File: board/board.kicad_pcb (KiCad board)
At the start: 2 copper layers, 21 x 13 mm, 1 part

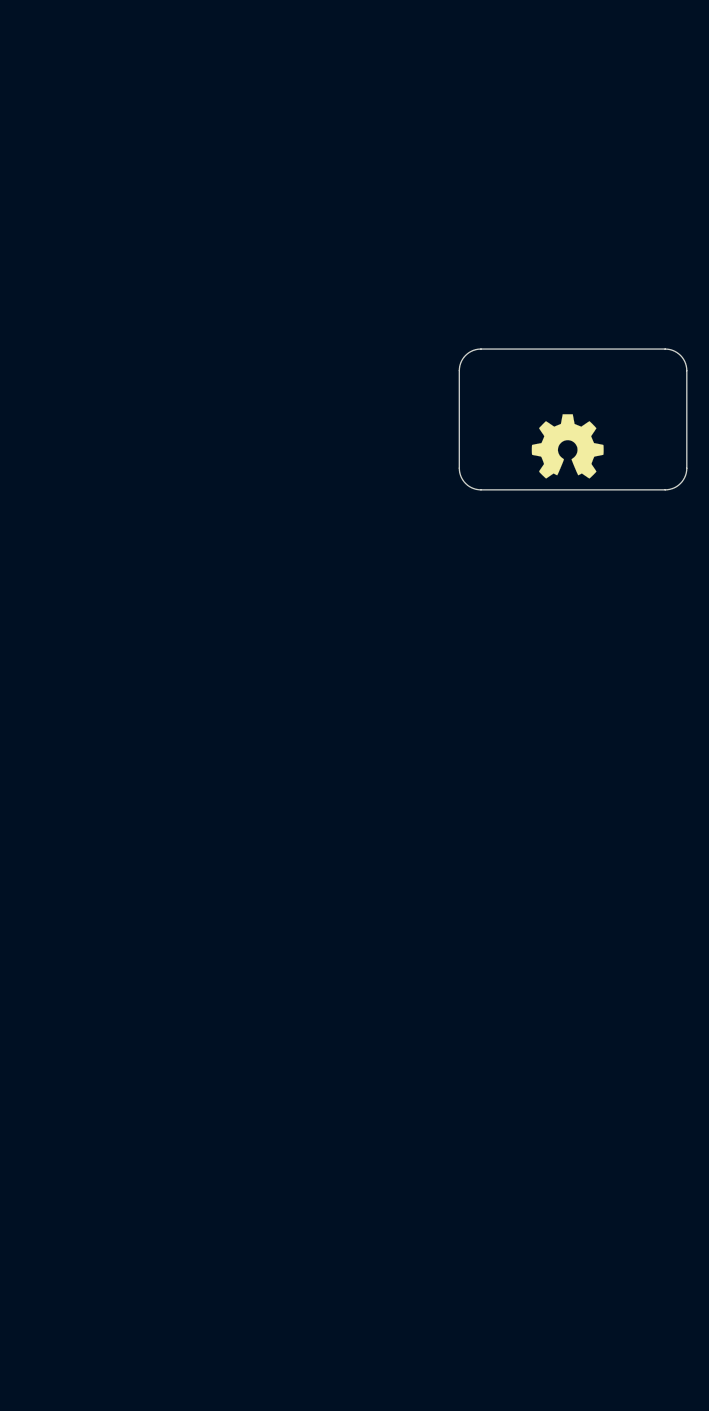
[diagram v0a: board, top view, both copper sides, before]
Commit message: fixed I2C bugs
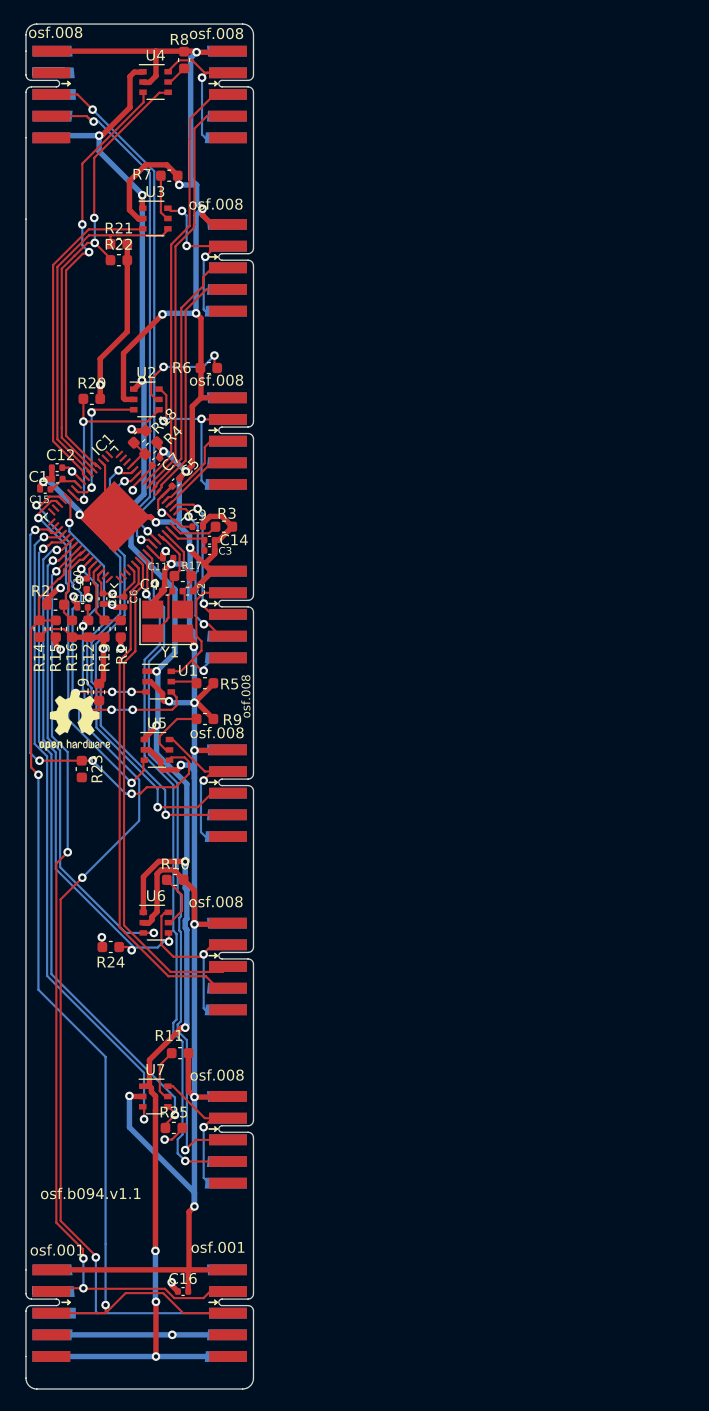
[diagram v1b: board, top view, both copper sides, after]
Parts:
- removed LOGO1: Logo_Open_Hardware_Small, Symbol:OSHW-Symbol_6.7x6mm_SilkScreen
- added C1: 100nF, Capacitor_SMD:C_0402_1005Metric, F.Cu at (102.9, 102.0)
- added C10: 100nF, Capacitor_SMD:C_0402_1005Metric, F.Cu at (105.6, 111.7)
- added C11: 100nF, Capacitor_SMD:C_0402_1005Metric, F.Cu at (113.1, 109.3)
- added C12: 100nF, Capacitor_SMD:C_0402_1005Metric, F.Cu at (102.9, 101.0)
- added C13: 100nF, Capacitor_SMD:C_0402_1005Metric, F.Cu at (105.2, 113.8)
- added C14: 100nF, Capacitor_SMD:C_0402_1005Metric, F.Cu at (116.9, 107.7)
- added C15: 100nF, Capacitor_SMD:C_0402_1005Metric, F.Cu at (101.8, 103.0)
- added C16: 1uF, Capacitor_SMD:C_0402_1005Metric, F.Cu at (114.5, 177.0)
- added C2: 16pF, Capacitor_SMD:C_0402_1005Metric, F.Cu at (114.9, 112.3)
- added C3: 100nF, Capacitor_SMD:C_0402_1005Metric, F.Cu at (116.9, 108.6)
- added C4: 16pF, Capacitor_SMD:C_0402_1005Metric, F.Cu at (113.0, 112.3)
- added C5: 100nF, Capacitor_SMD:C_0402_1005Metric, F.Cu at (113.8, 102.3)
- added C6: 100nF, Capacitor_SMD:C_0402_1005Metric, F.Cu at (109.0, 113.3)
- added C7: 100nF, Capacitor_SMD:C_0402_1005Metric, F.Cu at (112.0, 100.4)
- added C8: 100nF, Capacitor_SMD:C_0402_1005Metric, F.Cu at (107.1, 113.0)
- added C9: 100nF, Capacitor_SMD:C_0402_1005Metric, F.Cu at (115.8, 106.4)
- added IC1: USB2517-JZX, Package_DFN_QFN:QFN-64-1EP_9x9mm_P0.5mm_EP4.7x4.7mm, F.Cu at (108.2, 105.5)
- added J1: 008_USB_2x2, on_edge:on_edge_2x05_device, F.Cu at (100.0, 66.5)
- added J10: 001_I2C, on_edge:on_edge_2x05_host, F.Cu at (121.0, 179.0)
- added J2: 008_USB_2x2, on_edge:on_edge_2x05_host, F.Cu at (121.0, 163.0)
- added J3: 008_USB_2x2, on_edge:on_edge_2x05_host, F.Cu at (121.0, 66.5)
- added J4: 008_USB_2x2, on_edge:on_edge_2x05_host, F.Cu at (121.0, 82.5)
- added J5: 008_USB_2x2, on_edge:on_edge_2x05_host, F.Cu at (121.0, 114.5)
- added J6: 008_USB_2x2, on_edge:on_edge_2x05_host, F.Cu at (121.0, 98.5)
- added J7: 008_USB_2x2, on_edge:on_edge_2x05_host, F.Cu at (121.0, 147.0)
- added J8: 008_USB_2x2, on_edge:on_edge_2x05_host, F.Cu at (121.0, 131.0)
- added J9: 001_I2C, on_edge:on_edge_2x05_device, F.Cu at (100.0, 179.0)
- added R1: 100k, Capacitor_SMD:C_0603_1608Metric, F.Cu at (108.8, 115.8)
- added R10: 20k, Capacitor_SMD:C_0603_1608Metric, F.Cu at (113.8, 139.0)
- added R11: 20k, Capacitor_SMD:C_0603_1608Metric, F.Cu at (114.2, 155.0)
- added R12: 100k, Capacitor_SMD:C_0603_1608Metric, F.Cu at (105.8, 115.8)
- added R13: d.n.p, Capacitor_SMD:C_0603_1608Metric, F.Cu at (107.2, 115.8)
- added R14: d.n.p, Capacitor_SMD:C_0603_1608Metric, F.Cu at (101.2, 115.8)
- added R15: 100k, Capacitor_SMD:C_0603_1608Metric, F.Cu at (102.8, 115.8)
- added R16: d.n.p, Capacitor_SMD:C_0603_1608Metric, F.Cu at (104.2, 115.8)
- added R17: 1M, Capacitor_SMD:C_0603_1608Metric, F.Cu at (114.5, 111.0)
- added R18: d.n.p, Capacitor_SMD:C_0603_1608Metric, F.Cu at (110.5, 98.1)
- added R19: 100k, Capacitor_SMD:C_0603_1608Metric, F.Cu at (106.8, 121.7)
- added R2: 100k, Capacitor_SMD:C_0603_1608Metric, F.Cu at (102.7, 113.6)
- added R20: 100k, Capacitor_SMD:C_0603_1608Metric, F.Cu at (106.1, 94.6)
- added R21: 100k, Capacitor_SMD:C_0603_1608Metric, F.Cu at (108.6, 80.3)
- added R22: 100k, Capacitor_SMD:C_0603_1608Metric, F.Cu at (108.6, 81.8)
- added R23: 100k, Capacitor_SMD:C_0603_1608Metric, F.Cu at (105.2, 128.8)
- added R24: 100k, Capacitor_SMD:C_0603_1608Metric, F.Cu at (107.8, 145.2)
- added R25: 100k, Capacitor_SMD:C_0603_1608Metric, F.Cu at (113.7, 161.9)
- added R3: 12k, Capacitor_SMD:C_0603_1608Metric, F.Cu at (118.3, 106.4)
- added R4: 12k, Capacitor_SMD:C_0603_1608Metric, F.Cu at (111.5, 99.2)
- added R5: 20k, Capacitor_SMD:C_0603_1608Metric, F.Cu at (116.5, 120.8)
- added R6: 20k, Capacitor_SMD:C_0603_1608Metric, F.Cu at (116.9, 91.8)
- added R7: 20k, Capacitor_SMD:C_0603_1608Metric, F.Cu at (113.2, 74.0)
- added R8: 20k, Capacitor_SMD:C_0603_1608Metric, F.Cu at (114.6, 63.3)
- added R9: 20k, Capacitor_SMD:C_0603_1608Metric, F.Cu at (116.5, 124.2)
- added U1: TPS2553DDBVR, Package_SO:TSOP-6_1.65x3.05mm_P0.95mm, F.Cu at (112.2, 120.7)
- added U2: TPS2553DDBVR, Package_SO:TSOP-6_1.65x3.05mm_P0.95mm, F.Cu at (111.1, 94.7)
- added U3: TPS2553DDBVR, Package_SO:TSOP-6_1.65x3.05mm_P0.95mm, F.Cu at (111.9, 78.0)
- added U4: TPS2553DDBVR, Package_SO:TSOP-6_1.65x3.05mm_P0.95mm, F.Cu at (112.0, 65.3)
- added U5: TPS2553DDBVR, Package_SO:TSOP-6_1.65x3.05mm_P0.95mm, F.Cu at (112.1, 127.0)
- added U6: TPS2553DDBVR, Package_SO:TSOP-6_1.65x3.05mm_P0.95mm, F.Cu at (112.0, 142.9)
- added U7: TPS2553DDBVR, Package_SO:TSOP-6_1.65x3.05mm_P0.95mm, F.Cu at (111.9, 159.0)
- added Y1: Crystal_GND24_Small, Oscillator:Oscillator_SMD_Abracon_ASE-4Pin_3.2x2.5mm_HandSoldering, F.Cu at (113.1, 115.2)
- added l1: Logo_Open_Hardware_Large, Symbol:OSHW-Logo2_7.3x6mm_SilkScreen, F.Cu at (104.5, 124.3)
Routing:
- net GND: track 0.00 -> 336.2 mm, vias 0 -> 27
- net /hub/3.3v: track 0.00 -> 186.0 mm, vias 0 -> 13
- net /hub/5V: track 0.00 -> 163.2 mm, vias 0 -> 10
- net /hub/~reset: track 0.00 -> 96.0 mm, vias 0 -> 4
- net /hub/SCL: track 0.00 -> 94.5 mm, vias 0 -> 2
- net /hub/SDA: track 0.00 -> 88.4 mm, vias 0 -> 4
- net /hub/p6_m: track 0.00 -> 63.3 mm, vias 0 -> 2
- net /hub/fault6: track 0.00 -> 62.8 mm, vias 0 -> 2
- net /hub/p6_p: track 0.00 -> 62.7 mm, vias 0 -> 2
- net /hub/pwren6: track 0.00 -> 61.5 mm, vias 0 -> 2
- net /hub/fault5: track 0.00 -> 48.4 mm, vias 0 -> 3
- net /hub/up_p: track 0.00 -> 47.7 mm, vias 0 -> 2
- net /hub/up_m: track 0.00 -> 47.1 mm, vias 0 -> 2
- net /hub/p5_m: track 0.00 -> 46.7 mm
- net /hub/p5_p: track 0.00 -> 46.2 mm
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- added copper zone on In1.Cu, net /hub/3.3v
- added copper zone on In2.Cu, net GND
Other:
- board size 21 x 13 mm -> 21 x 126 mm
- copper layers 2 -> 4
- rule pad_to_mask_clearance: 0 -> 0.051
- board text added: "osf.001"
- board text added: "osf.008"
- board text added: "osf.b094.v1.1"
